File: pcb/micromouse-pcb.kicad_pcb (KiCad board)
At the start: 4 copper layers, 100 x 120 mm, 163 parts, among them J1 BATT_IN_1S, J2 EXT_SWITCH, J5 MOTOR_A_N20_ENCODER, J6 MOTOR_B_N20_ENCODER, J7 USB-C rear (GCT USB4105; VBUS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, J8 JTAG_1x6 (3V3,TMS,TCK,TDO,TDI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, Q1 Q_PMOS low-Vth (e.g. DMP2035U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, Q10 PT11-21B/L41 940nm 1206 photo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, Q11 PT11-21B/L41 940nm 1206 photo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, Q12 PT11-21B/L41 940nm 1206 photo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, Q13 PT11-21B/L41 940nm 1206 photo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, Q14 PT11-21B/L41 940nm 1206 photo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, Q15 PT11-21B/L41 940nm 1206 photo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, Q16 BSS138 (real part; Q_NMOS_GSD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, Q17 BSS138 (real part; Q_NMOS_GSD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, Q18 BSS138 (real part; Q_NMOS_GSD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, Q19 BSS138 (real part; Q_NMOS_GSD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, Q2 SFH309, Q20 BSS138 (real part; Q_NMOS_GSD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, Q21 BSS138 (real part; Q_NMOS_GSD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, Q22 BSS138 (real part; Q_NMOS_GSD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, Q23 BSS138 (real part; Q_NMOS_GSD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, Q24 BSS138 (real part; Q_NMOS_GSD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, Q25 BSS138 (real part; Q_NMOS_GSD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, Q26 BSS138 (real part; Q_NMOS_GSD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, Q27 BSS138 (real part; Q_NMOS_GSD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, Q28 BSS84 (PMOS indicator driver;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, Q29 BSS84 (PMOS indicator driver;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, Q3 SFH309, Q30 BSS84 (PMOS indicator driver;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, Q31 BSS84 (PMOS indicator driver;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, Q32 BSS84 (PMOS indicator driver;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, Q33 BSS84 (PMOS indicator driver;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, Q4 SFH309, Q5 SFH309, Q6 SFH309, Q7 SFH309, Q8 PT11-21B/L41 940nm 1206 photo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, Q9 PT11-21B/L41 940nm 1206 photo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, SW1 BTN_A (start / BOOT), SW2 RESET, SW3 BTN_B, SW4 BTN_C, U1 TPS63001 (fixed 3.3V buck-boo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, U2 TB6612FNG, U3 ESP32-S3-WROOM-1-N16 (non-R8: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, U4 CD74HC4067M, U6 USBLC6-2SC6 (SOT-23-6; 2P6 ba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

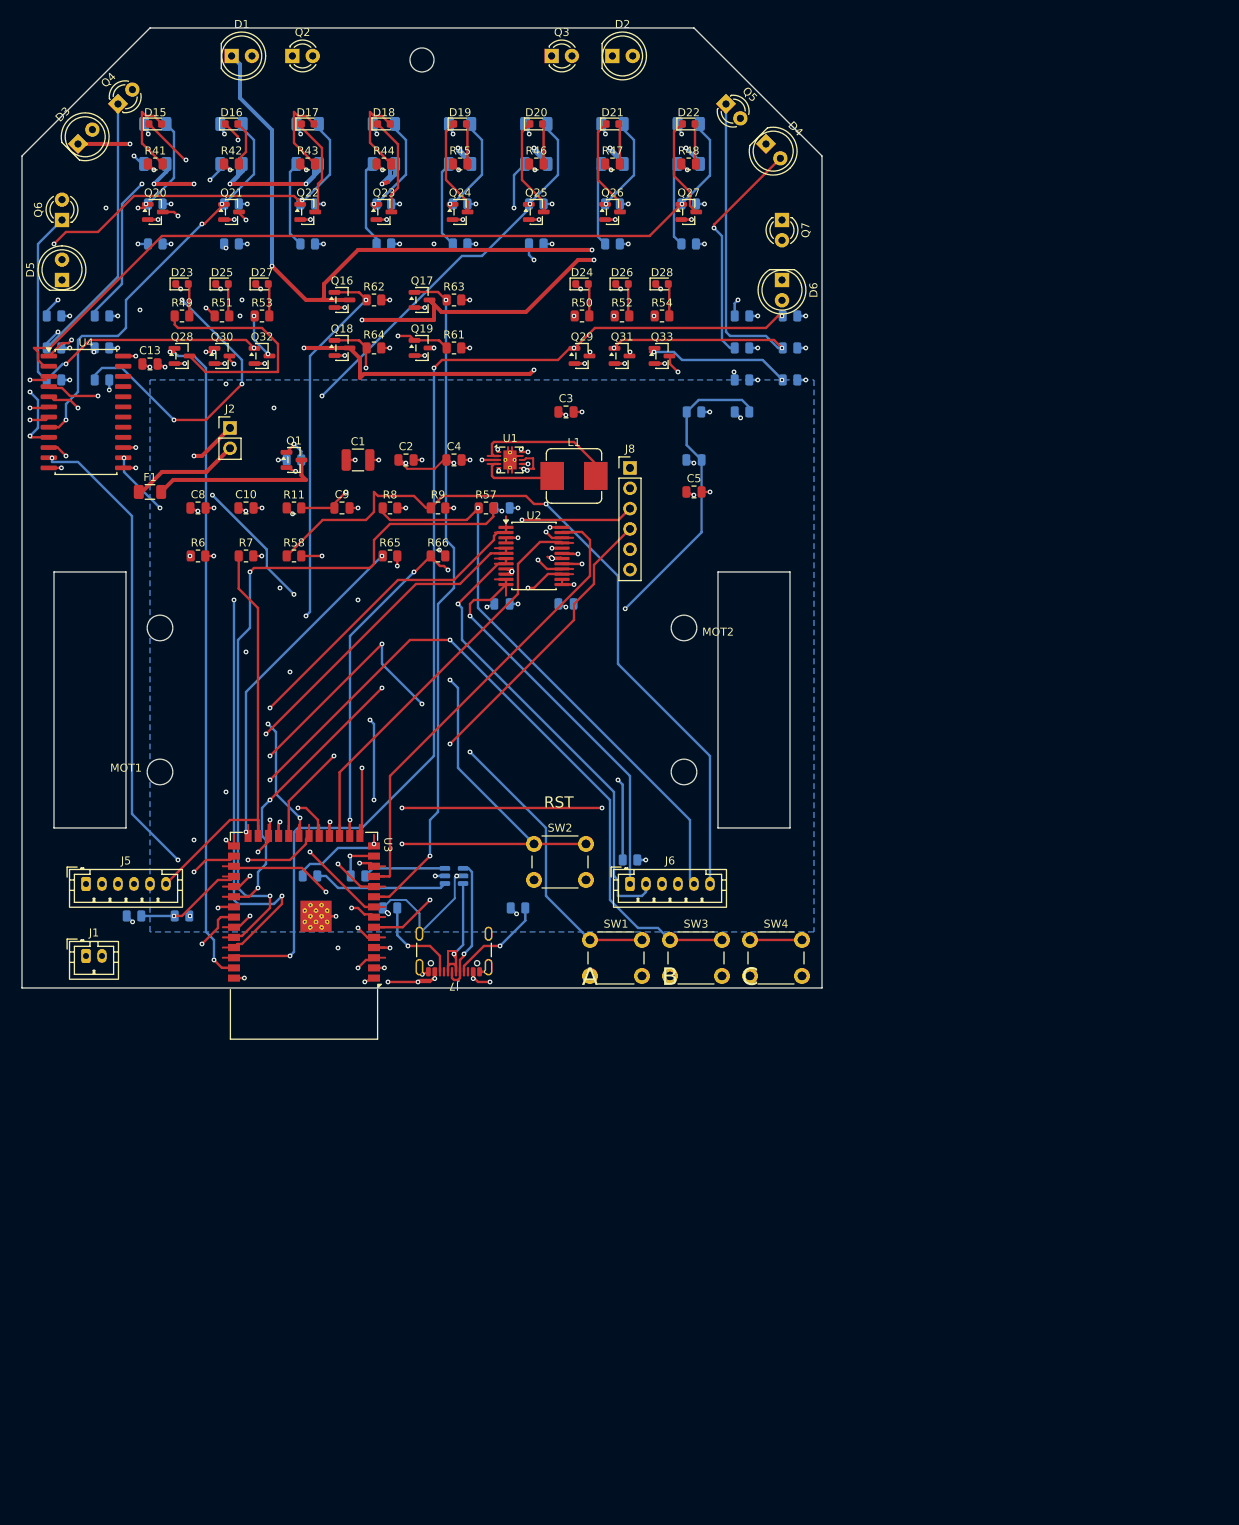
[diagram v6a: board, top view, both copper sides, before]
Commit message: Rev 5.3: routed to zero, wire-level verification, firmware + host sim
Board: rear-facing USB-C, soft EN switch (SW5), JTAG at rear, per-sensor
wall indicator LEDs, inboard bent-lead wall optics with silkscreen body
outlines, open edge wheel notches, India-available optos (TCRT5000 line,
PT334-6B wall). DRC 0 violations / 0 unconnected / 0 parity; ERC 0.

Verification: 28/28 netlist-computed circuit tests (TEST_REPORT.md),
trace-level copper analysis with pad-junction/T-split graph physics
(TRACE_REPORT.md), 30 firmware pins gated against the netlist, host sim
of the shipped control core passes all scenarios (caught 2 real control
bugs pre-hardware). Fab gates ALL PASSED; 42-line verified-MPN BOM.

Firmware: fw/micromouse (pins.h, control core, .ino with LEDC/PCNT/mux
scan/pulsed emitters), fw/sim host simulation, fw/check_pins.py gate.

Co-Authored-By: Claude Fable 5 <noreply@anthropic.com>
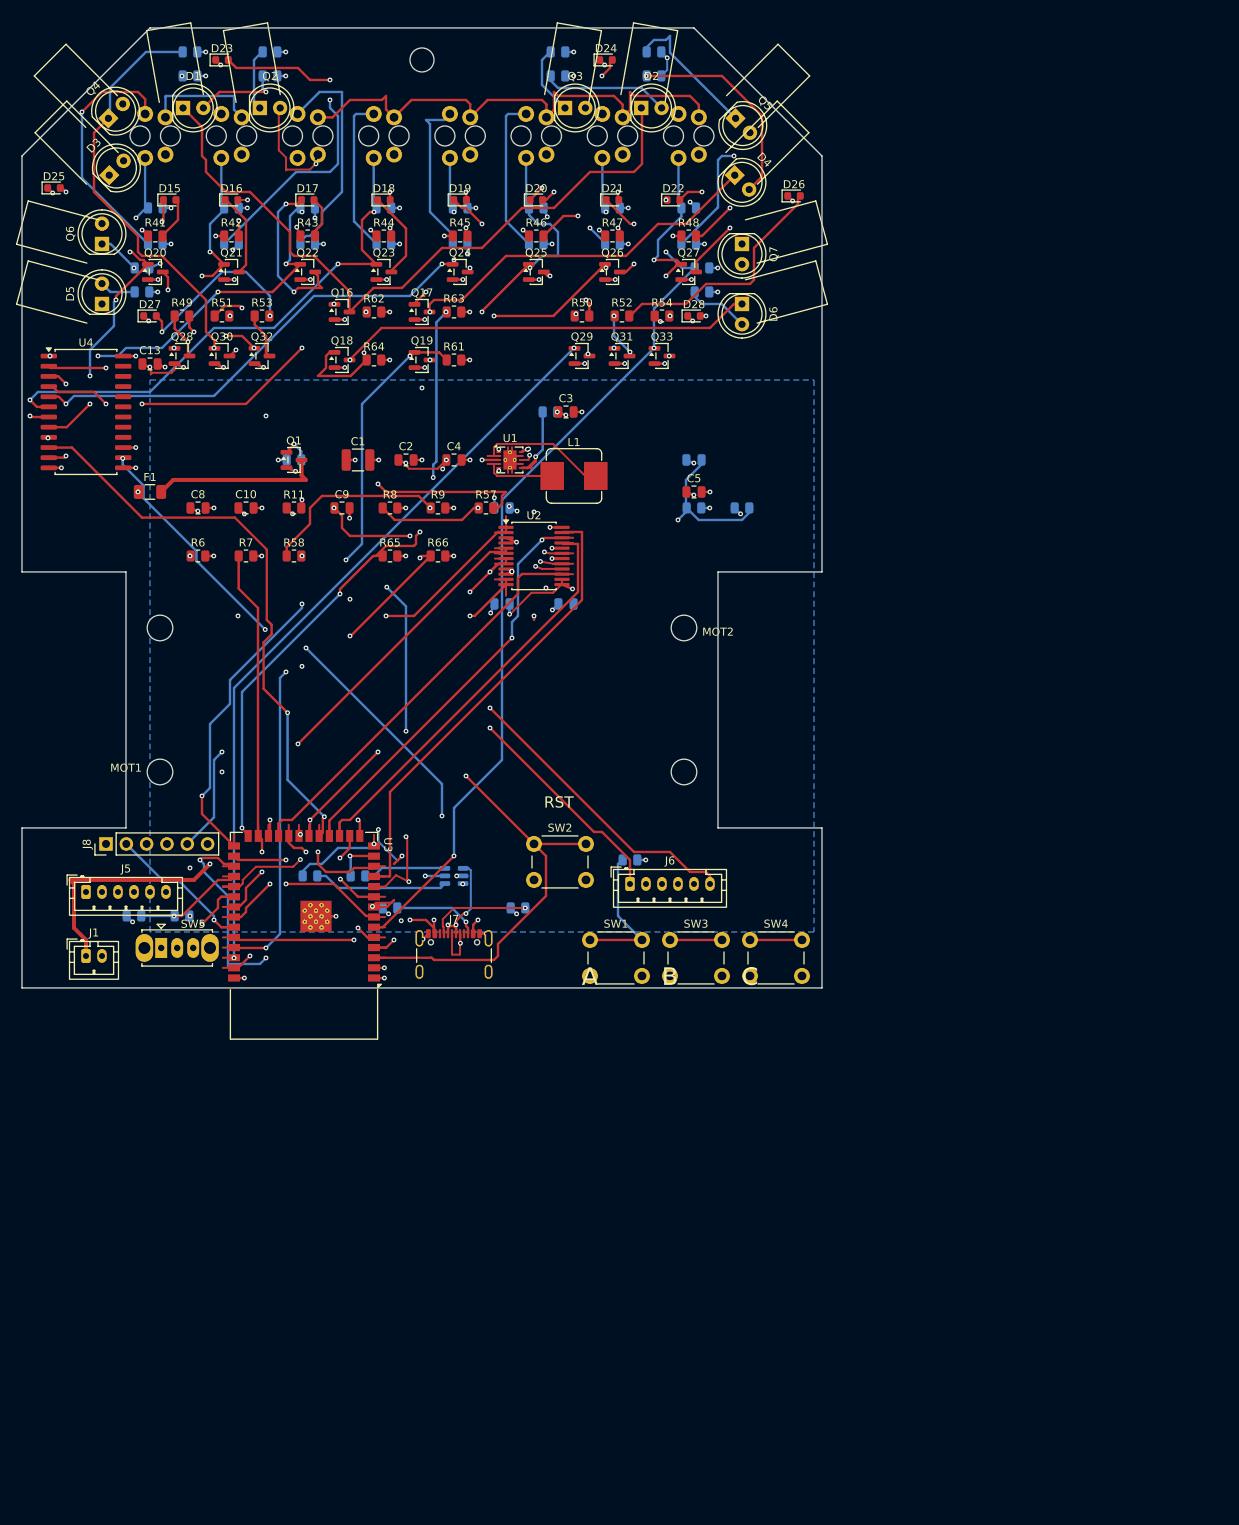
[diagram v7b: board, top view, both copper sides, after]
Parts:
- removed D10, D11, D12, D13, D14, D7, D8, D9: IR11-21C 940nm 1206 IR emitter (LD271 sym for ERC), LED_1206_3216Metric
- removed J2: EXT_SWITCH, PinHeader_1x02_P2.54mm_Vertical
- removed Q10, Q11, Q12, Q13, Q14, Q15, Q8, Q9: PT11-21B/L41 940nm 1206 phototransistor, DAYLIGHT-FILTERED 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, LED_1206_3216Metric
- added LS1: TCRT5000, TCRT5000, B.Cu at (16.7, 13.5)
- added LS2: TCRT5000, TCRT5000, B.Cu at (26.2, 13.5)
- added LS3: TCRT5000, TCRT5000, B.Cu at (35.7, 13.5)
- added LS4: TCRT5000, TCRT5000, B.Cu at (45.2, 13.5)
- added LS5: TCRT5000, TCRT5000, B.Cu at (54.8, 13.5)
- added LS6: TCRT5000, TCRT5000, B.Cu at (64.3, 13.5)
- added LS7: TCRT5000, TCRT5000, B.Cu at (73.8, 13.5)
- added LS8: TCRT5000, TCRT5000, B.Cu at (83.3, 13.5)
- added R69: R_0805_2012Metric, R_0805_2012Metric, B.Cu at (66.0, 48.0)
- added SW5: SW_Slide_SPDT_Straight_CK_OS102011MS2Q, SW_Slide_SPDT_Straight_CK_OS102011MS2Q, F.Cu at (17.4, 115.0)
- C10: value 10uF -> C_0805_2012Metric
- C13, C6, C8: value 100nF -> C_0805_2012Metric
- C9: value 1uF -> C_0805_2012Metric
- D1, D2, D3, D4, D5, D6: value SFH4550 (THT, LD271 base symbol) -> LED_D5.0mm_IRGrey
- D15, D16, D17, D18, D19, D20, D21, D22: value Indicator LED 0603 super-red AlInGaP, high-efficiency bin REQUIRED at 1.4mA (e.g. Kingbright APT1608SURCK; LD271 base s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 -> LED_0603_1608Metric
- D23, D24, D25, D26, D27, D28: value Indicator LED 0603 super-red AlInGaP, high-eff bin (e.g. APT1608SURCK) -> LED_0603_1608Metric
- F1: value 2A_resettable -> Fuse_1206_3216Metric
- J1: value BATT_IN_1S -> JST_PH_B2B-PH-K_1x02_P2.00mm_Vertical
- J5: value MOTOR_A_N20_ENCODER -> JST_PH_B6B-PH-K_1x06_P2.00mm_Vertical
- J6: value MOTOR_B_N20_ENCODER -> JST_PH_B6B-PH-K_1x06_P2.00mm_Vertical
- J7: value USB-C rear (GCT USB4105; VBUS unused -- battery powers the board) -> USB_C_Receptacle_GCT_USB4105-xx-A_16P_TopMnt_Horizontal
- J8: value JTAG_1x6 (3V3,TMS,TCK,TDO,TDI,GND) -> PinHeader_1x06_P2.54mm_Vertical
- Q1: value Q_PMOS low-Vth (e.g. DMP2035U-7) -> SOT-23
- Q16, Q17, Q18, Q19, Q20, Q21, Q22, Q23, Q24, Q25, Q26, Q27: value BSS138 (real part; Q_NMOS_GSD base symbol used so ERC checks pins) -> SOT-23
- Q2, Q3, Q4, Q5, Q6, Q7: value SFH309 -> LED_D5.0mm_IRBlack; footprint LED_D3.0mm_Clear -> LED_D5.0mm_IRBlack
- Q28, Q29, Q30, Q31, Q32, Q33: value BSS84 (PMOS indicator driver; Q_PMOS base symbol) -> SOT-23
- R1, R61, R62, R63, R64: value 100k -> R_0805_2012Metric
- R10, R11, R6, R65, R66, R67, R7, R8, R9: value 10k -> R_0805_2012Metric
- R12, R56: value 5.1k -> R_0805_2012Metric
- R13, R15, R17, R19, R21, R23, R25, R27, R29, R31, R33, R35, R37, R39: value 47k -> R_0805_2012Metric
- R14, R16, R18, R20, R22, R24: value 33 -> R_0805_2012Metric
- R2: value 22k -> R_0805_2012Metric
- R26, R28, R30, R32, R34, R36, R38, R40: value 120 -> R_0805_2012Metric
- R3: value 33k -> R_0805_2012Metric
- R41, R42, R43, R44, R45, R46, R47, R48, R49, R50, R51, R52, R53, R54, R57, R58: value 1k -> R_0805_2012Metric
- R59, R60: value 22 -> R_0805_2012Metric
- R68: value 15k -> R_0805_2012Metric
- SW1: value BTN_A (start / BOOT) -> SW_PUSH_6mm
- SW2: value RESET -> SW_PUSH_6mm
- SW3: value BTN_B -> SW_PUSH_6mm
- SW4: value BTN_C -> SW_PUSH_6mm
- U1: value TPS63001 (fixed 3.3V buck-boost; TPS63000 base symbol so ERC checks pins) -> Texas_DRC0010J_ThermalVias
- U2: value TB6612FNG -> SSOP-24_5.3x8.2mm_P0.65mm
- U3: value ESP32-S3-WROOM-1-N16 (non-R8: octal-PSRAM variants lose IO35-37 = buttons 2/3) -> ESP32-S3-WROOM-1
- U4: value CD74HC4067M -> SOIC-24W_7.5x15.4mm_P1.27mm
- U6: value USBLC6-2SC6 (SOT-23-6; 2P6 base symbol so ERC checks pins) -> SOT-23-6
- moved J8 80.6 mm to (10.5, 102.0), turned to 90 degrees
- moved R15 43.9 mm to (67.0, 3.00)
- moved R13 42.6 mm to (31.0, 3.00)
- moved R17 40.7 mm to (21.0, 3.00)
- moved R19 40.7 mm to (79.0, 3.00)
- moved R16 37.8 mm to (67.0, 6.00)
- moved R14 36.6 mm to (31.0, 6.00)
- moved R18 35.7 mm to (21.0, 6.00)
- moved R20 35.7 mm to (79.0, 6.00)
- moved D23 28.4 mm to (25.0, 4.00)
- moved D24 28.2 mm to (73.0, 4.00)
- moved D25 24.2 mm to (4.00, 20.0)
- moved D26 24.2 mm to (96.5, 21.0)
- moved R21 17.8 mm to (15.0, 30.0)
- moved R23 17.8 mm to (85.0, 30.0)
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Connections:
- F1 pad 1: Net-(J2-Pin_2) -> Net-(J1-Pin_1)
- U1 pad 6: VM_BATT -> PWR_EN
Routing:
- net PWR_EN: track 0.00 -> 110.1 mm, vias 0 -> 2
- net JTAG_TDI: track 106.5 -> 42.3 mm, vias 4 -> 2
- net JTAG_TMS: track 79.2 -> 19.5 mm
- net JTAG_TCK: track 79.0 -> 20.3 mm, vias 4 -> 1
- net Net-(D23-A): track 4.05 -> 57.1 mm, vias 0 -> 2
- net MUX_S1: track 78.5 -> 130.8 mm
- net MOTB_N: track 61.0 -> 113.0 mm, vias 1 -> 3
- net Net-(D5-A): track 54.6 -> 4.52 mm, vias 3 -> 0
- net JTAG_TDO: track 88.7 -> 39.8 mm, vias 2 -> 1
- net Net-(D24-A): track 4.05 -> 48.1 mm, vias 0 -> 2
- net WALL2_SENSE: track 178.2 -> 134.6 mm, vias 4 -> 2
- net USER_BTN2: track 109.0 -> 66.6 mm, vias 4 -> 1
- net Net-(D3-A): track 57.4 -> 21.5 mm, vias 2 -> 1
- net Net-(LS2-Pad1): track 12.5 -> 42.8 mm, vias 2 -> 1
- net Net-(D1-A): track 40.6 -> 10.8 mm
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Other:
- outline, holes or cut-outs redrawn
